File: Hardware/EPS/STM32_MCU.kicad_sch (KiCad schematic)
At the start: 22 parts

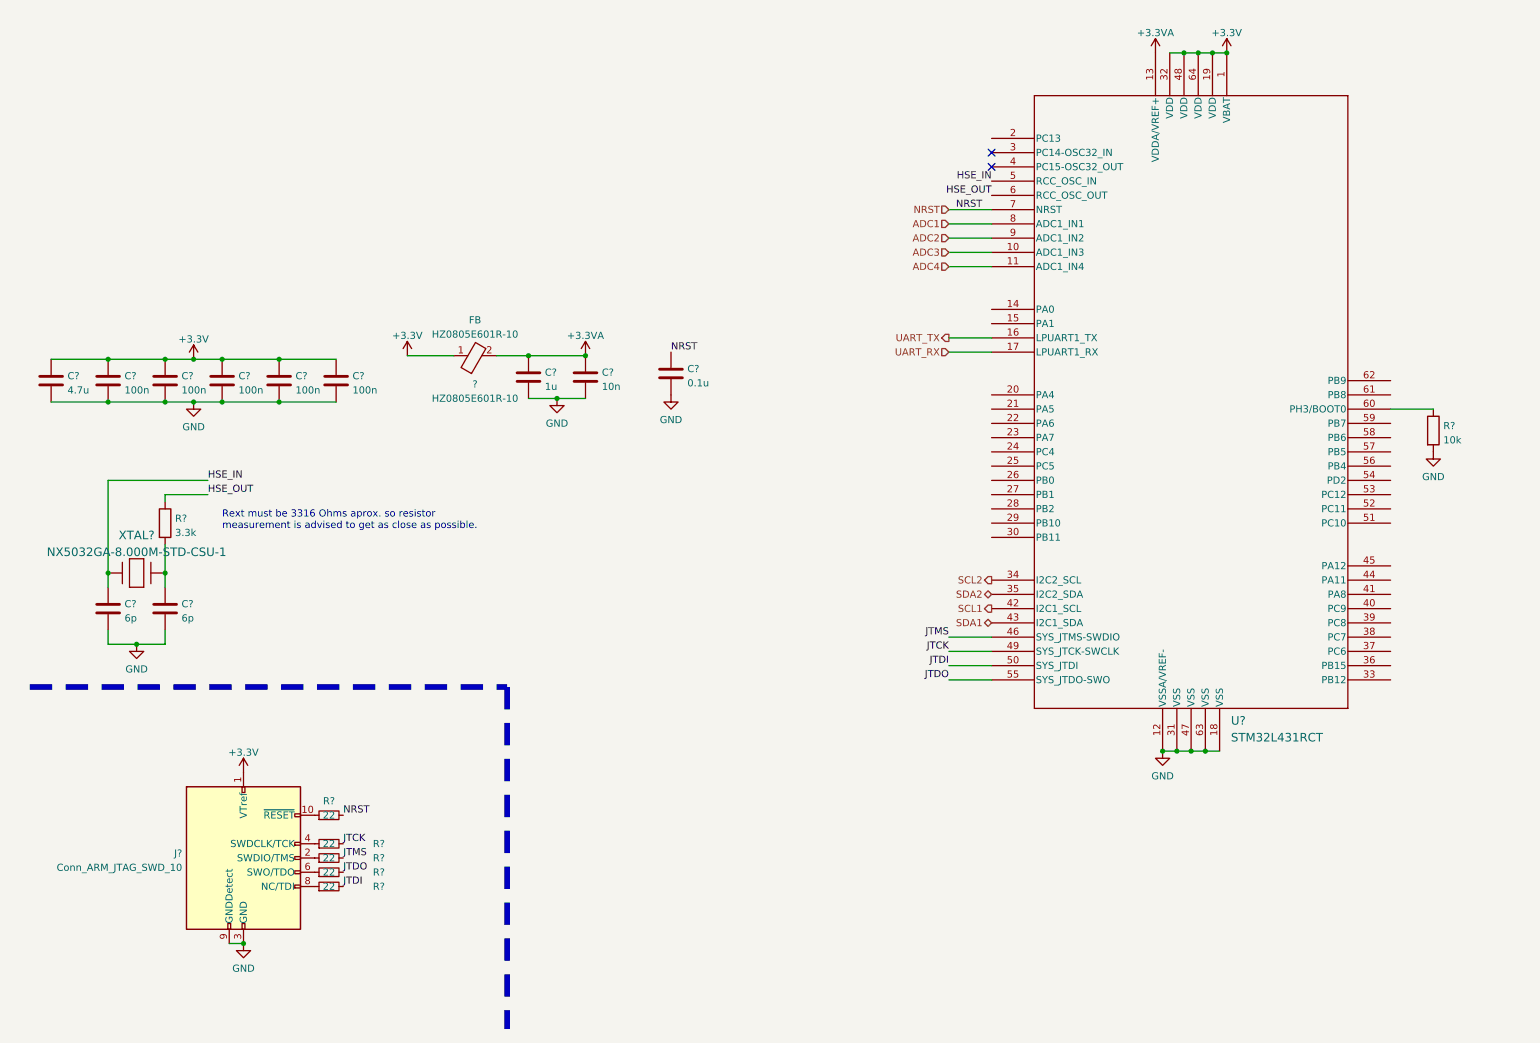
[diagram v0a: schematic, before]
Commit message: Fuse, Power Switch to 3.3V, connector ESD Prot.
v0.0.2
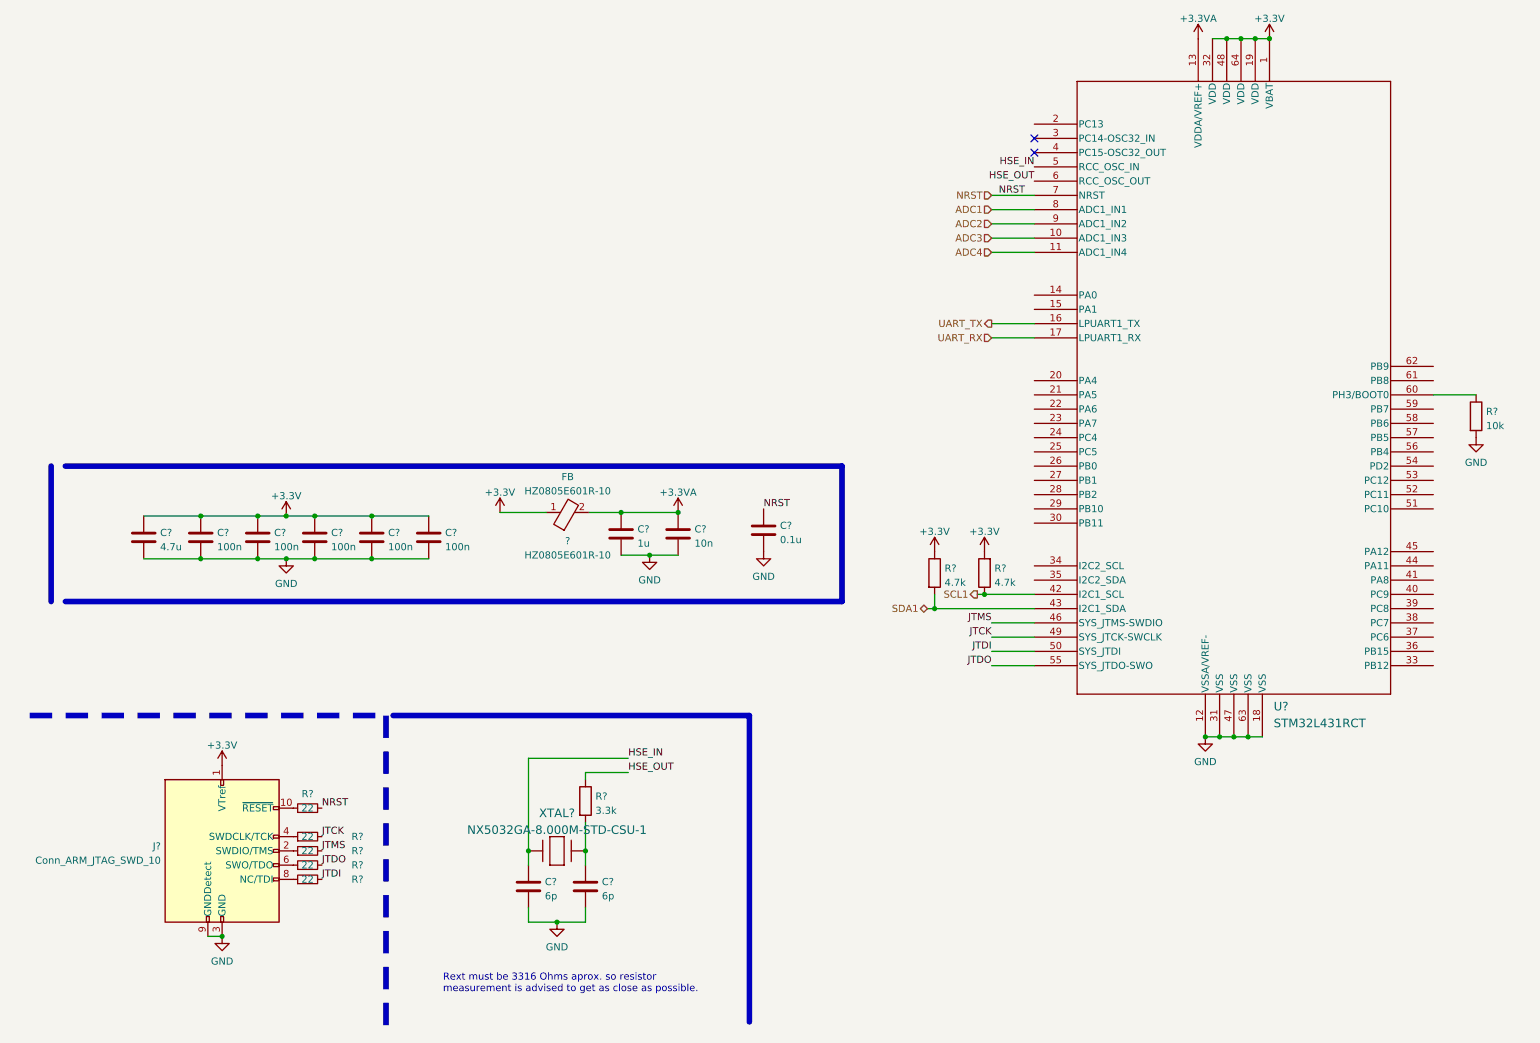
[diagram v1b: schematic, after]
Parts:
- added R? (x2): 4.7k, symbol Device:R
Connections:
- net +3.3V: now also R?.1, R?.2
- net SCL1: now also R?.1
- net SDA1: now also R?.2
- net SCL2: no longer names the net of U?.34 (I2C2_SCL)
- net SDA2: no longer names the net of U?.35 (I2C2_SDA)
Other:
- title: (none) -> EPS Schematics
- moved on the sheet: ?, C?, J?, R?, U?, XTAL?

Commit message: Defined pinout for board connector, major revision
v0.0.3 - Fixed erratas and cleaned the schematic
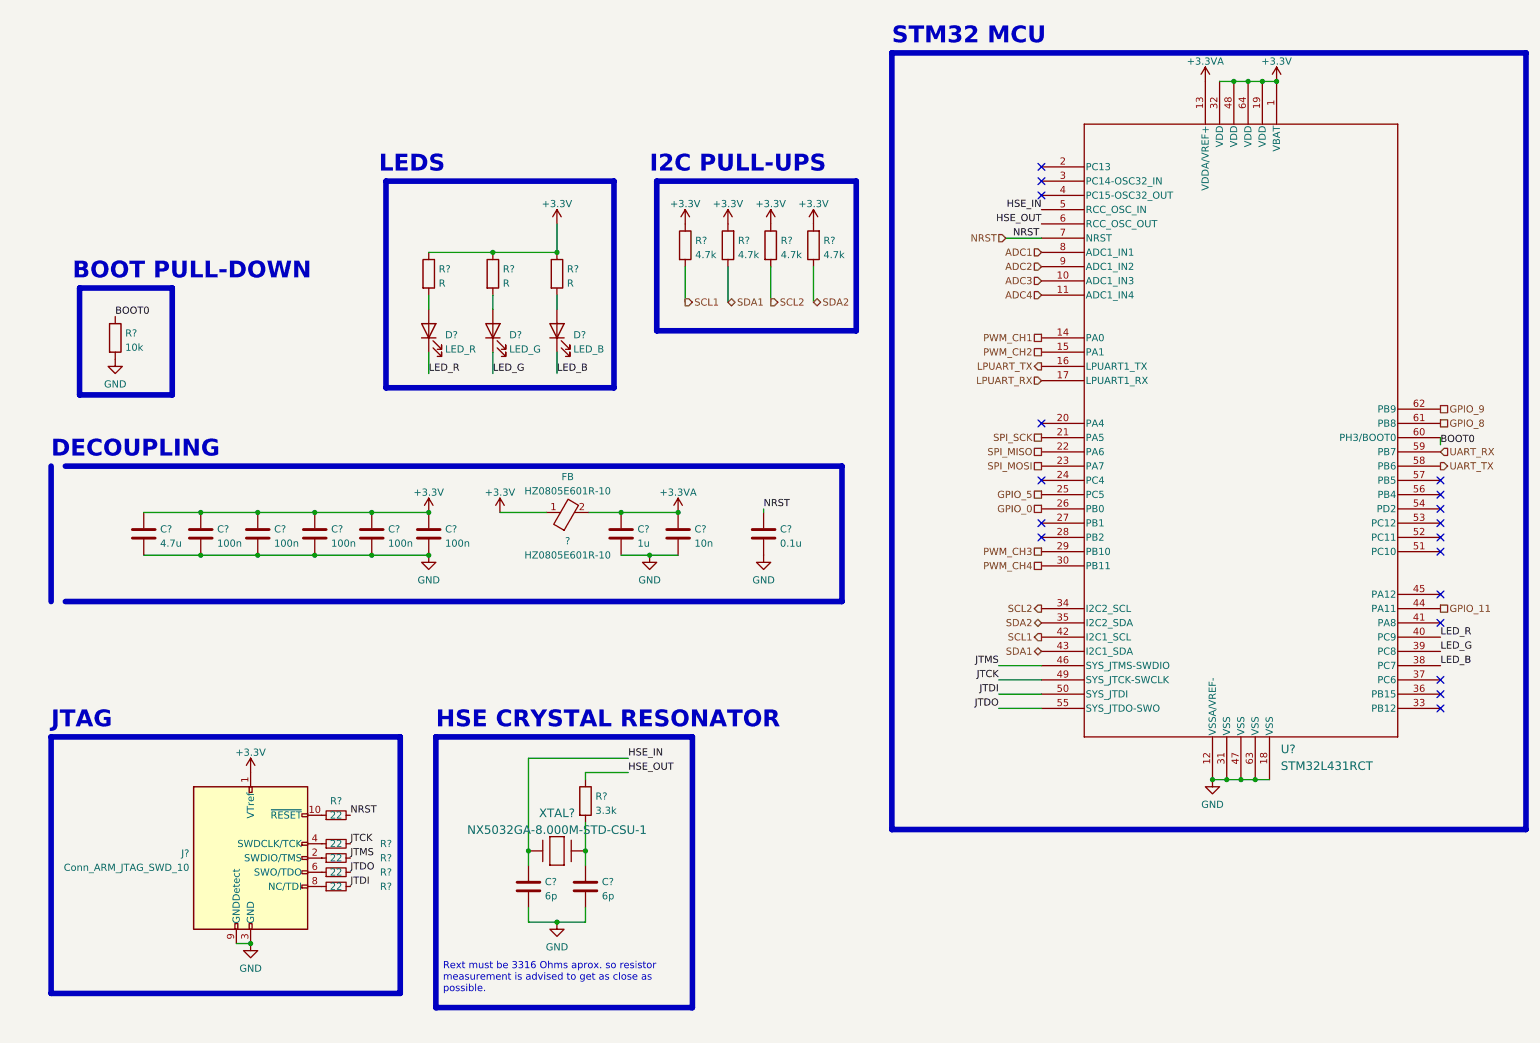
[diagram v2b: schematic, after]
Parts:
- removed R? (x2): 4.7k, symbol Device:R
- removed R?: 10k, symbol Device:R
- added D?: LED_B, symbol Device:LED
- added D?: LED_G, symbol Device:LED
- added D?: LED_R, symbol Device:LED
- added R? (x4): 4.7k, symbol Device:R
- added R? (x3): R, symbol Device:R
- added R?: 10k, symbol Device:R
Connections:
- net +3.3V: now also R?.1, R?.1, R?.1, R?.1, R?.1, R?.2, R?.2
- net GND: now also R?.2
- net SCL1: now also R?.2
- net SDA1: now also R?.1
- net UART_RX: now also U?.59 (PB7); no longer U?.17 (LPUART1_RX)
- net UART_TX: now also U?.58 (PB6); no longer U?.16 (LPUART1_TX)
- net PWM_CH1: now reaches U?.14 (PA0)
- net PWM_CH2: now reaches U?.15 (PA1)
- net SPI_SCK: now reaches U?.21 (PA5)
- net SPI_MISO: now reaches U?.22 (PA6)
- net SPI_MOSI: now reaches U?.23 (PA7)
- net GPIO_5: now reaches U?.25 (PC5)
- net GPIO_0: now reaches U?.26 (PB0)
- net PWM_CH3: now reaches U?.29 (PB10)
- net PWM_CH4: now reaches U?.30 (PB11)
- net SCL2: now reaches U?.34 (I2C2_SCL)
- net SCL2: now also R?.2
- net SDA2: now reaches U?.35 (I2C2_SDA)
- net SDA2: now also R?.1
- net LED_B: now reaches U?.38 (PC7)
- net LED_B: now also D?.1 (K)
- net LED_G: now reaches U?.39 (PC8)
- net LED_G: now also D?.1 (K)
- net LED_R: now reaches U?.40 (PC9)
- net LED_R: now also D?.1 (K)
- net GPIO_11: now reaches U?.44 (PA11)
- net BOOT0: now reaches U?.60 (PH3/BOOT0)
- net BOOT0: now also R?.1
- net GPIO_8: now reaches U?.61 (PB8)
- net GPIO_9: now reaches U?.62 (PB9)
- new net: D?.2 (A), R?.2 (x3)
- new net LPUART_RX: U?.17 (LPUART1_RX)
- new net LPUART_TX: U?.16 (LPUART1_TX)
- no-connect marks 2 -> 18
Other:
- note added: "BOOT PULL-DOWN"
- note added: "DECOUPLING"
- note added: "HSE CRYSTAL RESONATOR"
- note added: "I2C PULL-UPS"
- note added: "JTAG"
- note added: "LEDS"
- note added: "STM32 MCU"
- moved on the sheet: C?, J?, R?, U?
